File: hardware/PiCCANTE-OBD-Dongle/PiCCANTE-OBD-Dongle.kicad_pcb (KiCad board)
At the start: 4 copper layers, 50 x 60 mm, 38 parts, among them J1 Micro_SD_Card, U1 SN65HVD230, U2 SN65HVD230, U3 SN65HVD230, U4 TPS5430DDA

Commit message: Switch out TRX / "Improve" Routing
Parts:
- removed G*** (x2): LOGO, LOGO
- removed JCAN0Term1, JCAN1Term1: ~, Connector_PinHeader_2.54mm:PinHeader_1x02_P2.54mm_Vertical
- removed R3: 120, PCM_Resistor_SMD_AKL:R_0201_0603Metric
- removed R4, R6: 22K, Resistor_SMD:R_0201_0603Metric
- removed U3: SN65HVD230, Package_SO:SOIC-8_3.9x4.9mm_P1.27mm
- added JCAN2Term0: ~, Connector_PinHeader_2.54mm:PinHeader_1x02_P2.54mm_Vertical, F.Cu at (99.7, 74.0)
- added JCAN2Term1: ~, Connector_PinHeader_2.54mm:PinHeader_1x02_P2.54mm_Vertical, F.Cu at (102.3, 91.0)
- added U5: TCAN3413DR, EasyEDA:SOP-8_L4.9-W3.9-P1.27-LS6.0-BL-1, F.Cu at (101.8, 101.6)
- C3: footprint Capacitor_SMD:CP_Elec_4x5.4 -> PCM_Capacitor_SMD_AKL:C_1206_3216Metric
- C4: value 220µF -> 220uF; footprint Capacitor_SMD:CP_Elec_6.3x5.4_Nichicon -> PCM_Capacitor_SMD_AKL:C_1206_3216Metric
- R1: value 22K -> 120
- U1, U2: value SN65HVD230 -> TCAN3413DR; footprint Package_SO:SOIC-8_3.9x4.9mm_P1.27mm -> EasyEDA:SOP-8_L4.9-W3.9-P1.27-LS6.0-BL-1
- moved R1 25.7 mm to (102.5, 96.5), turned to 90 degrees
- moved U1 17.0 mm to (101.5, 84.5), turned to 90 degrees
- moved U2 15.5 mm to (102.0, 69.0), turned to 90 degrees
- moved R12 10.1 mm to (134.5, 92.3)
- moved R13 10.1 mm to (134.5, 95.5)
- moved R2 8.66 mm to (102.0, 79.7), turned to 90 degrees
- moved R5 4.53 mm to (102.5, 109.5), turned to 90 degrees
- moved C4 2.83 mm to (136.0, 88.0)
- moved D2 2.55 mm to (142.0, 89.0), turned to 180 degrees
- moved C3 1.92 mm to (142.5, 109.0)
- moved L1 1.00 mm to (139.0, 94.5)
- moved JCAN2Term2 0.55 mm to (102.3, 107.0)
- moved R15 0.50 mm to (139.0, 108.0)
- moved R14 0.18 mm to (134.0, 108.0)
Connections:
- JCAN2Term2 pad 2: CAN2L -> CAN2H
- R1 pad 1: CAN_LOW_PWR -> CAN1L
- R1 pad 2: GND -> Net-(JCAN2Term1-Pin_1)
- R2 pad 1: CAN0H -> CAN0L
- R5 pad 1: CAN2H -> CAN2L
- U1 pad 1: CAN0TX -> CAN1TX
- U1 pad 4: CAN0RX -> CAN1RX
- U1 pad 5: unconnected-(U1-Vref-Pad5) -> +3.3V
- U1 pad 6: CAN0L -> CAN1L
- U1 pad 7: CAN0H -> CAN1H
- U2 pad 1: CAN1TX -> CAN0TX
- U2 pad 4: CAN1RX -> CAN0RX
- U2 pad 5: unconnected-(U2-Vref-Pad5) -> +3.3V
- U2 pad 6: CAN1L -> CAN0L
- U2 pad 7: CAN1H -> CAN0H
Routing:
- net +3.3V: track 15.2 -> 48.3 mm, vias 12 -> 9
- net Net-(D2-A): track 23.3 -> 2.65 mm
- net GND: track 49.3 -> 38.1 mm, vias 32 -> 26
- net Net-(U4-VSENSE): track 3.70 -> 12.6 mm
- net CAN0H: track 14.5 -> 9.21 mm
- net Net-(JCAN2Term1-Pin_1): track 0.00 -> 5.27 mm
- net CAN2H: track 15.2 -> 10.7 mm
- net CAN1H: track 15.1 -> 11.0 mm
- net CAN2L: track 16.7 -> 20.7 mm, vias 1 -> 0
- net CAN0RX: track 10.2 -> 7.10 mm
- net Net-(JCAN2Term0-Pin_2): track 2.71 -> 5.44 mm
- net Net-(JCAN1Term1-Pin_1): track 2.71 -> 0.00 mm
- net CAN0TX: track 8.08 -> 5.64 mm
- net CAN_LOW_PWR: track 57.7 -> 55.4 mm
- net CAN1L: track 15.6 -> 17.6 mm, vias 1 -> 0
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- added copper zone on F.Cu, net Net-(D2-A)
- added copper zone on In2.Cu, net VSYS
- removed copper zone on B.Cu, net VSYS
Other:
- board text removed: "(symbol "LOGO" (pin_names (offset 1.016)) (in_bom yes) (on_board yes) (property "Reference" "#G" (at 0 2.36521 0) (effects (font (size 1.27 1.27)) hide) ) (property "Value" "LOGO" (at 0 -2.36521 0) (effects (font (size 1.27 1.27)) hide) ) (property "Footprint" "" (at 0 0 0) (effects (font (size 1.27 1.27)) hide) ) (property "Datasheet" "" (at 0 0 0) (effects (font (size 1.27 1.27)) hide) ) (symbo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"
- board text removed: "(symbol "LOGO" (pin_names (offset 1.016)) (in_bom yes) (on_board yes) (property "Reference" "#G" (at 0 56.769 0) (effects (font (size 1.27 1.27)) hide) ) (property "Value" "LOGO" (at 0 -56.769 0) (effects (font (size 1.27 1.27)) hide) ) (property "Footprint" "" (at 0 0 0) (effects (font (size 1.27 1.27)) hide) ) (property "Datasheet" "" (at 0 0 0) (effects (font (size 1.27 1.27)) hide) ) (symbol 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"

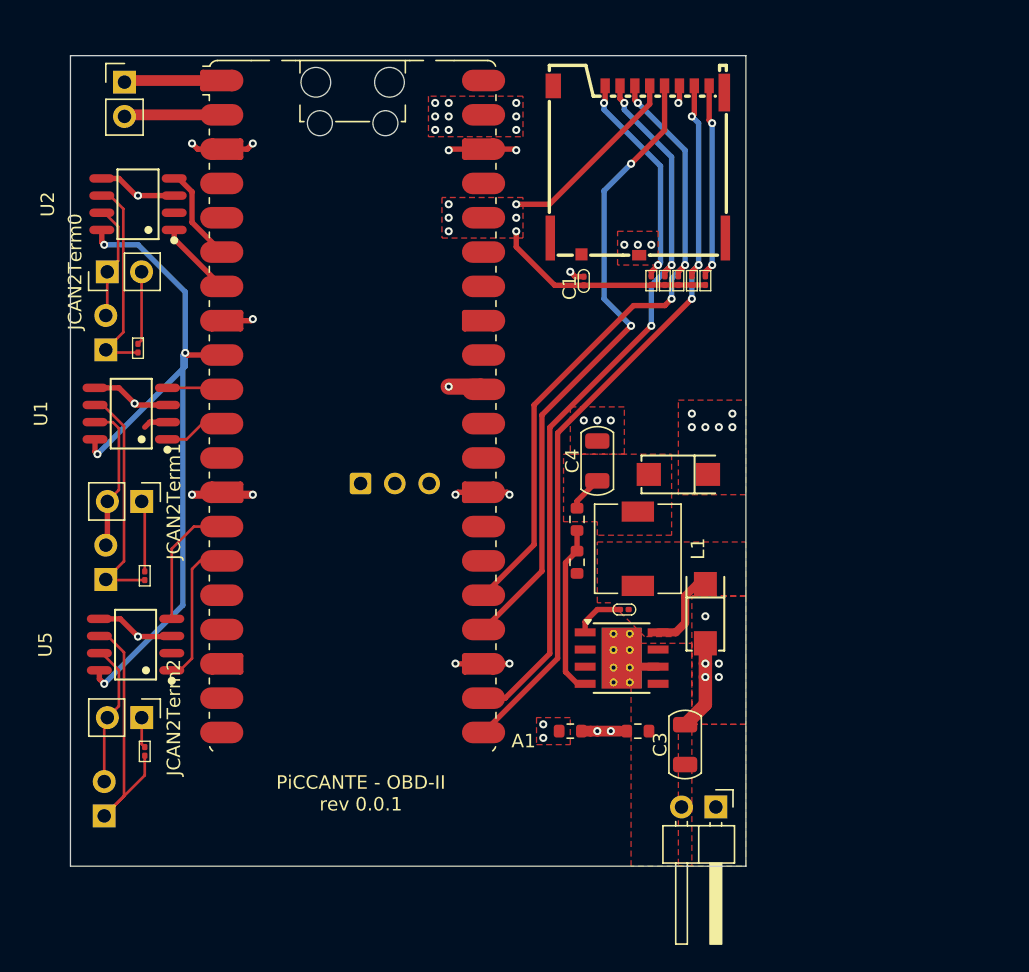
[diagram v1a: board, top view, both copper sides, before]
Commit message: Put pico on the other side
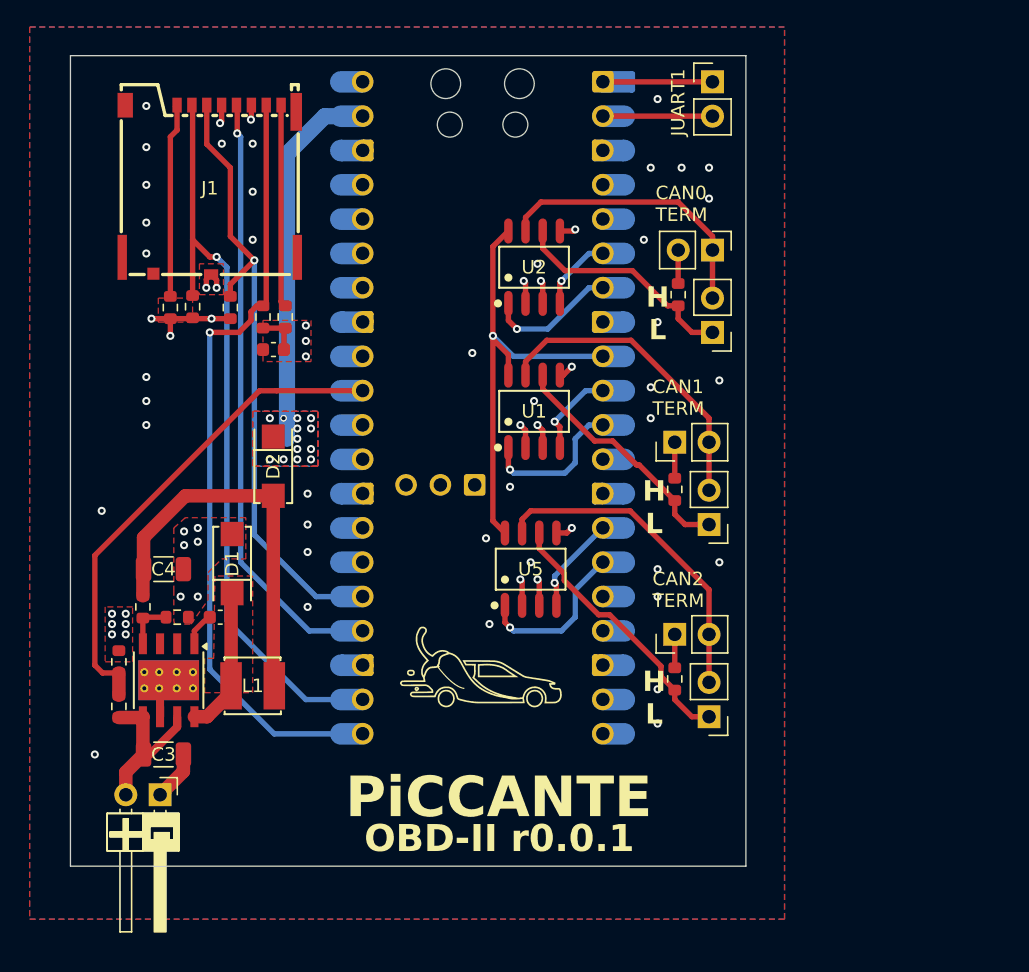
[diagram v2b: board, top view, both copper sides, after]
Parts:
- added G***: LOGO, LOGO, F.Cu at (127.4, 103.3)
- added G***: LOGO, LOGO, B.Cu at (106.8, 81.2)
- A1: footprint PiCO_CUSTOM_KEEPOUT:RaspberryPi_Pico_W_SMD_HandSolder_CUSTOM_KEEPOUT -> PiCO_CUSTOM_KEEPOUT:RaspberryPi_Pico_W_SMD_THT_COMBO_CUSTOM_KEEPOUT; moved to B.Cu
- C1, C2: footprint PCM_Capacitor_SMD_AKL:C_0201_0603Metric -> Capacitor_SMD:C_0603_1608Metric
- C3, C4: footprint PCM_Capacitor_SMD_AKL:C_1206_3216Metric -> Capacitor_SMD:C_1206_3216Metric
- JCAN0, JCAN1, JCAN2: footprint Connector_PinHeader_2.54mm:PinHeader_1x02_P2.54mm_Horizontal -> Connector_PinHeader_2.54mm:PinHeader_1x02_P2.54mm_Vertical; moved to F.Cu
- L1: footprint Inductor_SMD:L_6.3x6.3_H3 -> EasyEDA:IND-SMD_L4.0-W4.0
- R1, R10, R11, R2, R5, R7, R8, R9: footprint PCM_Resistor_SMD_AKL:R_0201_0603Metric -> Resistor_SMD:R_0603_1608Metric
- moved JCAN2 45.4 mm to (144.3, 106.9), turned to 180 degrees
- moved JCAN0 44.9 mm to (144.5, 78.5), turned to 180 degrees
- moved JCAN1 44.8 mm to (144.3, 92.7), turned to 180 degrees
- moved JCAN2Term0 44.8 mm to (144.5, 72.4), turned to -90 degrees
- moved JUART1 43.5 mm to (144.5, 59.9)
- moved JPWR1 41.1 mm to (103.6, 112.7)
- moved R2 40.2 mm to (142.0, 75.7)
- moved JCAN2Term2 39.9 mm to (141.7, 100.8), turned to 90 degrees
- moved R1 39.7 mm to (141.7, 90.1)
- moved JCAN2Term1 39.7 mm to (141.7, 86.6), turned to 90 degrees
- moved R5 39.6 mm to (141.7, 104.1)
- moved C3 38.6 mm to (103.9, 109.7), turned to 0 degrees
- moved R15 38.5 mm to (100.6, 106.2), turned to 90 degrees
- moved R7 35.7 mm to (104.4, 76.6)
- moved D1 35.2 mm to (109.0, 95.6), turned to 90 degrees
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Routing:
- net +3.3V: track 48.3 -> 21.0 mm, vias 9 -> 13
- net VSYS: track 0.00 -> 27.3 mm, vias 15 -> 13
- net Net-(D2-A): track 2.65 -> 29.3 mm
- net GND: track 38.1 -> 15.5 mm, vias 26 -> 58
- net CAN_LOW_PWR: track 55.4 -> 35.3 mm, vias 4 -> 1
- net CAN2H: track 10.7 -> 24.4 mm
- net VBATT: track 0.00 -> 12.2 mm
- net CAN1H: track 11.0 -> 23.0 mm
- net CAN0H: track 9.21 -> 20.9 mm
- net Net-(U4-VSENSE): track 12.6 -> 3.64 mm
- net CAN1TX: track 4.50 -> 11.2 mm, vias 0 -> 1
- net Net-(D1-K): track 6.22 -> 10.7 mm
- net CAN0TX: track 5.64 -> 9.77 mm, vias 0 -> 1
- net Net-(A1-GPIO16): track 55.8 -> 58.9 mm, vias 3 -> 1
- net Net-(JCAN2Term0-Pin_2): track 5.44 -> 2.41 mm
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- added copper zone on B.Cu, net GND
- added copper zone on B.Cu, net VSYS
- removed copper zone on F.Cu, net Net-(D2-A)
- removed copper zone on F.Cu, net VBATT
- removed copper zone on In2.Cu, net VSYS
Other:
- board text added: "+"
- board text added: "-"
- board text added: "CAN0 TERM"
- board text added: "CAN1 TERM"
- board text added: "CAN2 TERM"
- board text added: "H L"
- board text added: "JPWR1"
- board text added: "JUART1"
- board text added: "OBD-II r0.0.1"
- board text added: "PiCCANTE ️️️️"
- board text removed: "PiCCANTE - OBD-II rev 0.0.1"
